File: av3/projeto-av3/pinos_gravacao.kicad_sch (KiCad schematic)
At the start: 0 parts

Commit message: Esquemático finalizado, faltando somente o PCB.
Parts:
- added J18: Conn_02x03_Odd_Even, Connector_PinHeader_2.54mm:PinHeader_2x03_P2.54mm_Vertical_SMD, symbol Connector_Generic:Conn_02x03_Odd_Even
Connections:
- new net +5V: J18.2 (Pin_2)
- new net GND: J18.6 (Pin_6)
- new net MISO: J18.1 (Pin_1)
- new net MOSI: J18.4 (Pin_4)
- new net SCK: J18.3 (Pin_3)
- new net reset: J18.5 (Pin_5)

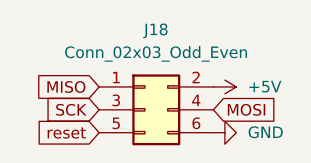
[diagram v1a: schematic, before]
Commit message: Referencias de componentes resetados; Progresso de 20% no PCB;
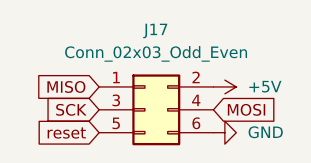
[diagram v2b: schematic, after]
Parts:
- renumbered J18 to J17
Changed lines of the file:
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@@
 		(dnp no)
 		(fields_autoplaced yes)
-		(property "Reference" "#PWR077"
+		(property "Reference" "#PWR051"
 			(at 63.5 52.07 0)
 			(effects
@@
 			(project "av3"
 				(path "/82998b71-606c-4e03-99b7-477e2a65cb94/f171beb6-5f8e-4da6-bc78-acb2437bd512"
-					(reference "#PWR077")
+					(reference "#PWR051")
 					(unit 1)
 				)
@@
 		(dnp no)
 		(fields_autoplaced yes)
-		(property "Reference" "#PWR076"
+		(property "Reference" "#PWR050"
 			(at 53.34 46.99 0)
 			(effects
@@
 			(project "av3"
 				(path "/82998b71-606c-4e03-99b7-477e2a65cb94/f171beb6-5f8e-4da6-bc78-acb2437bd512"
-					(reference "#PWR076")
+					(reference "#PWR050")
 					(unit 1)
 				)
@@
 		(dnp no)
 		(fields_autoplaced yes)
-		(property "Reference" "J18"
+		(property "Reference" "J17"
 			(at 50.8 40.64 0)
 			(effects
@@
 			(project "av3"
 				(path "/82998b71-606c-4e03-99b7-477e2a65cb94/f171beb6-5f8e-4da6-bc78-acb2437bd512"
-					(reference "J18")
+					(reference "J17")
 					(unit 1)
 				)
